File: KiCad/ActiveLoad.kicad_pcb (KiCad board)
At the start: 2 copper layers, 80 x 70 mm, 59 parts, among them J1 AuxPower, J2 TWI, J3 PDI, J4 TC74X-3.3, J5 PowerInput, J6 FAN, Q1 BC807, Q2 BC817, Q4 BD136, U1 LM78L33, U2 L78M12, U3 ATXMEGA32E5-AU, U4 LM358, U5 TL081

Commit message: PCB
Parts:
- removed C1: 47u, Capacitors_SMD:CP_Elec_6.3x5.8
- removed Q1: BC807, TO_SOT_Packages_SMD:SOT-23
- removed R3: 13, Resistors_SMD:R_0805
- added D1: 1N4148, Diodes_SMD:D_1206, B.Cu at (94.6, 87.6)
- added Q3: BD911, TO_SOT_Packages_THT:TO-220-3_Vertical, B.Cu at (81.9, 59.1)
- added ROT1: ROTARY-ENCODER, sparkfun:SF-ROTARY-ENCODER, F.Cu at (104.8, 79.4)
- added SW1: SW_SPDT, JPConnectors:SlideSwitch3Poles, F.Cu at (62.9, 48.9)
- added SW2: SW_SPDT, JPConnectors:SlideSwitch3Poles, F.Cu at (52.7, 74.3)
- C10, C11, C12, C13, C14, C15, C16, C17, C18, C2, C3, C4, C5, C6, C7, C8, C9, J6, L1, Q2, Q4, R1, R10, R11, R12, R13, R14, R15, R16, R17, R18, R19, R2, R20, R21, R22, R23, R26, R4, R5, R6, R7, R8, R9, U2, U3, U4, U5: moved to B.Cu
- J3: footprint Pin_Headers:Pin_Header_Straight_2x03_Pitch2.54mm -> Pin_Headers:Pin_Header_Angled_2x03_Pitch2.54mm; moved to B.Cu
- U1: value LM78L33 -> UA78M33; footprint TO_SOT_Packages_SMD:SOT-89-3 -> TO_SOT_Packages_SMD:TO-252-2; moved to B.Cu
- moved C2 160.5 mm to (54.0, 92.7), turned to 90 degrees
- moved C10 147.5 mm to (76.8, 95.9), turned to 90 degrees
- moved R14 146.7 mm to (75.6, 78.7), turned to 270 degrees
- moved R1 146.3 mm to (75.6, 69.8), turned to 180 degrees
- moved C9 141.9 mm to (65.4, 83.8), turned to 270 degrees
- moved R24 130.5 mm to (76.8, 31.8)
- moved C8 128.2 mm to (57.8, 78.1), turned to 270 degrees
- moved R26 127.4 mm to (85.7, 62.9), turned to 270 degrees
- moved C4 126.2 mm to (46.4, 84.5), turned to 180 degrees
- moved C16 124.9 mm to (92.1, 61.0), turned to 180 degrees
- moved U5 124.7 mm to (90.8, 64.8), turned to 180 degrees
- moved C5 123.1 mm to (89.5, 105.4), turned to 90 degrees
- moved C15 122.8 mm to (82.5, 83.8)
- moved R15 120.3 mm to (96.5, 62.9), turned to 90 degrees
- moved R25 120.0 mm to (76.2, 27.9)
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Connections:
- U1 pad 1: +3V3 -> Net-(C4-Pad1)
- U1 pad 3: Net-(C1-Pad1) -> +3V3
- U3 pad 11: Net-(U3-Pad11) -> ENC_A
- U3 pad 12: Net-(U3-Pad12) -> ENC_B
- U3 pad 29: Net-(U3-Pad29) -> CURRENT_LEVEL
- U3 pad 3: FAN_CONTROL -> DRAIN_CONTROL
- U3 pad 30: Net-(U3-Pad30) -> VOLTAGE_LEVEL
- U3 pad 4: DRAIN_CONTROL -> FAN_CONTROL
- U3 pad 9: Net-(U3-Pad9) -> ENC_Switch
- U4 pad 1: Net-(R16-Pad2) -> Net-(R12-Pad1)
- U4 pad 2: Net-(C14-Pad1) -> Net-(R13-Pad2)
- U4 pad 3: Net-(R12-Pad2) -> Net-(R17-Pad2)
- U4 pad 5: Net-(R17-Pad2) -> Net-(R12-Pad2)
- U4 pad 6: Net-(R13-Pad2) -> Net-(C14-Pad1)
- U4 pad 7: Net-(R12-Pad1) -> Net-(R16-Pad2)
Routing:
- net GND: track 0.00 -> 233.9 mm
- net +3V3: track 0.00 -> 142.0 mm, vias 0 -> 2
- net PowerInput: track 0.00 -> 76.6 mm
- net +12V: track 0.00 -> 72.1 mm, vias 0 -> 1
- net SDA: track 0.00 -> 68.0 mm, vias 0 -> 2
- net SCK: track 0.00 -> 66.5 mm, vias 0 -> 3
- net Net-(C4-Pad1): track 0.00 -> 53.5 mm
- net CURRENT_LEVEL: track 0.00 -> 41.7 mm
- net Net-(C18-Pad1): track 0.00 -> 41.5 mm
- net FAN_CONTROL: track 0.00 -> 38.0 mm, vias 0 -> 2
- net ENC_Switch: track 0.00 -> 31.1 mm
- net PDI_DATA: track 0.00 -> 26.2 mm, vias 0 -> 1
- net ENC_B: track 0.00 -> 24.7 mm
- net PDI_CLK: track 0.00 -> 21.9 mm, vias 0 -> 1
- net ENC_A: track 0.00 -> 20.6 mm
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- added copper zone on B.Cu, net GND
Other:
- net class Default: trace_width 0.25 -> 0.5; via_dia 0.6 -> 1.4; via_drill 0.4 -> 0.6
- net class HighCurrent added: clearance 0.3, trace_width 2, via_dia 2.4, via_drill 1
- net class Power added: clearance 0.2, trace_width 1, via_dia 1.6, via_drill 0.8

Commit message: Finishing touches
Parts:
- added REF**: MountingHole_3.5mm, Mounting_Holes:MountingHole_3.5mm, F.Cu at (48.5, 105.4)
- added REF**: MountingHole_3.5mm, Mounting_Holes:MountingHole_3.5mm, F.Cu at (109.0, 44.0)
- added REF**: MountingHole_3.5mm, Mounting_Holes:MountingHole_3.5mm, F.Cu at (48.5, 44.0)
- added REF**: MountingHole_3.5mm, Mounting_Holes:MountingHole_3.5mm, F.Cu at (109.0, 105.4)
- R20: footprint Resistors_THT:R_Axial_Power_L48.0mm_W12.5mm_P55.88mm -> JPResistors:R_Axial_Power_L48.0mm_W12.5mm_P50.8mm
- R24, R25: moved to B.Cu
- U1, U2: footprint TO_SOT_Packages_SMD:TO-252-2 -> TO_SOT_Packages_SMD:TO-252-2_Rectifier
- moved R25 74.9 mm to (74.9, 102.9), turned to 90 degrees
- moved R24 68.6 mm to (74.3, 100.3), turned to 180 degrees
- moved C9 3.81 mm to (65.4, 80.0)
- moved SW1 2.54 mm to (65.4, 48.9)
- moved R20 2.01 mm to (53.3, 49.5)
- moved C4 1.91 mm to (48.3, 84.5)
- moved J3 1.91 mm to (106.7, 99.1)
- moved C2 0.63 mm to (54.6, 92.7)
- moved J1 0.63 mm to (43.2, 63.5)
- moved J5 0.63 mm to (116.8, 63.5)
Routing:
- net GND: track 233.9 -> 386.3 mm, vias 0 -> 3
- net CURRENT_LEVEL: track 41.7 -> 111.2 mm, vias 0 -> 1
- net PowerInput: track 76.6 -> 130.9 mm, vias 0 -> 1
- net +3V3: track 142.0 -> 171.4 mm, vias 2 -> 5
- net Net-(J1-Pad2): track 19.9 -> 32.7 mm
- net VOLTAGE_LEVEL: track 0.00 -> 6.09 mm
- net Net-(C16-Pad1): track 5.98 -> 7.62 mm
- net +12V: track 72.1 -> 71.4 mm, vias 1 -> 2
- net Net-(C4-Pad1): track 53.5 -> 52.9 mm
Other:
- board text added: "0R1 15W"
- board text added: "ActiveLoad v1 2018.03.18, JP"
- board text added: "Aux Power"
- board text added: "Gnd"
- board text added: "Input Power"
- board text added: "bypass"

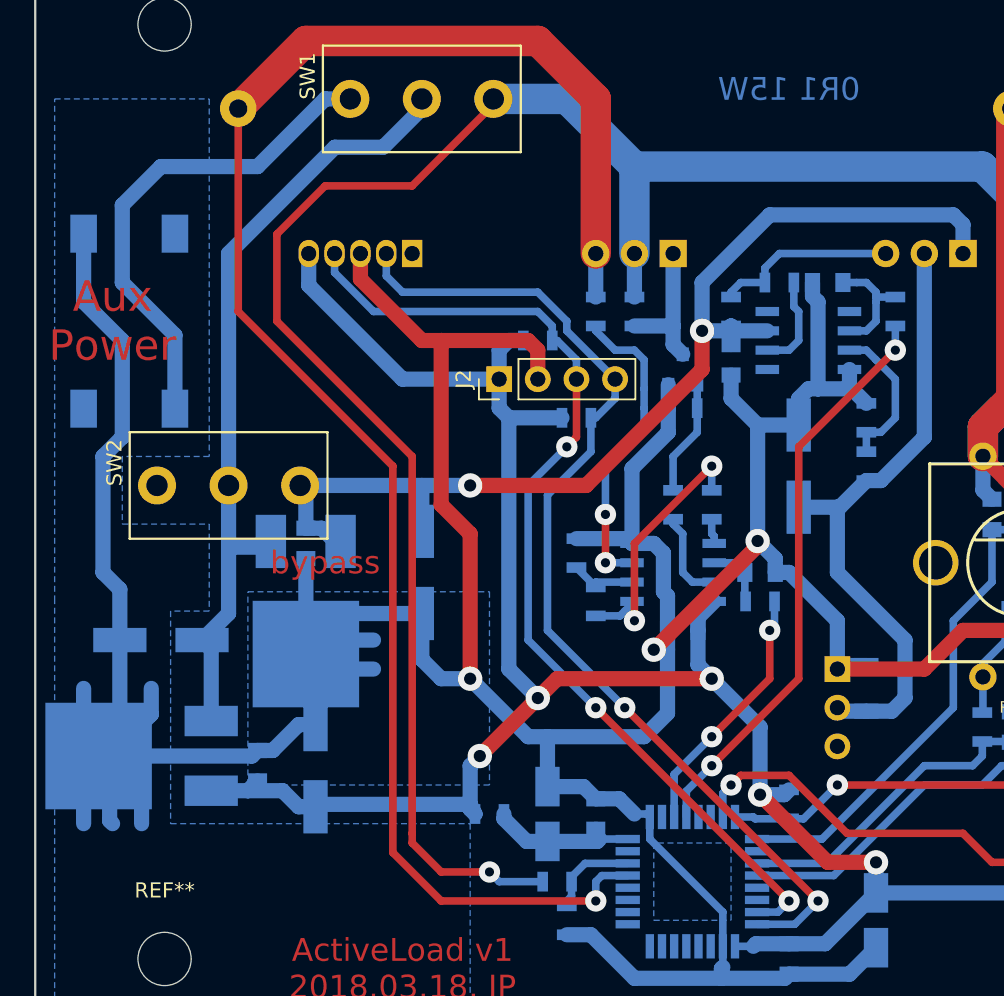
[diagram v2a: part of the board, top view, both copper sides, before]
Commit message: Diodes around 7812 added
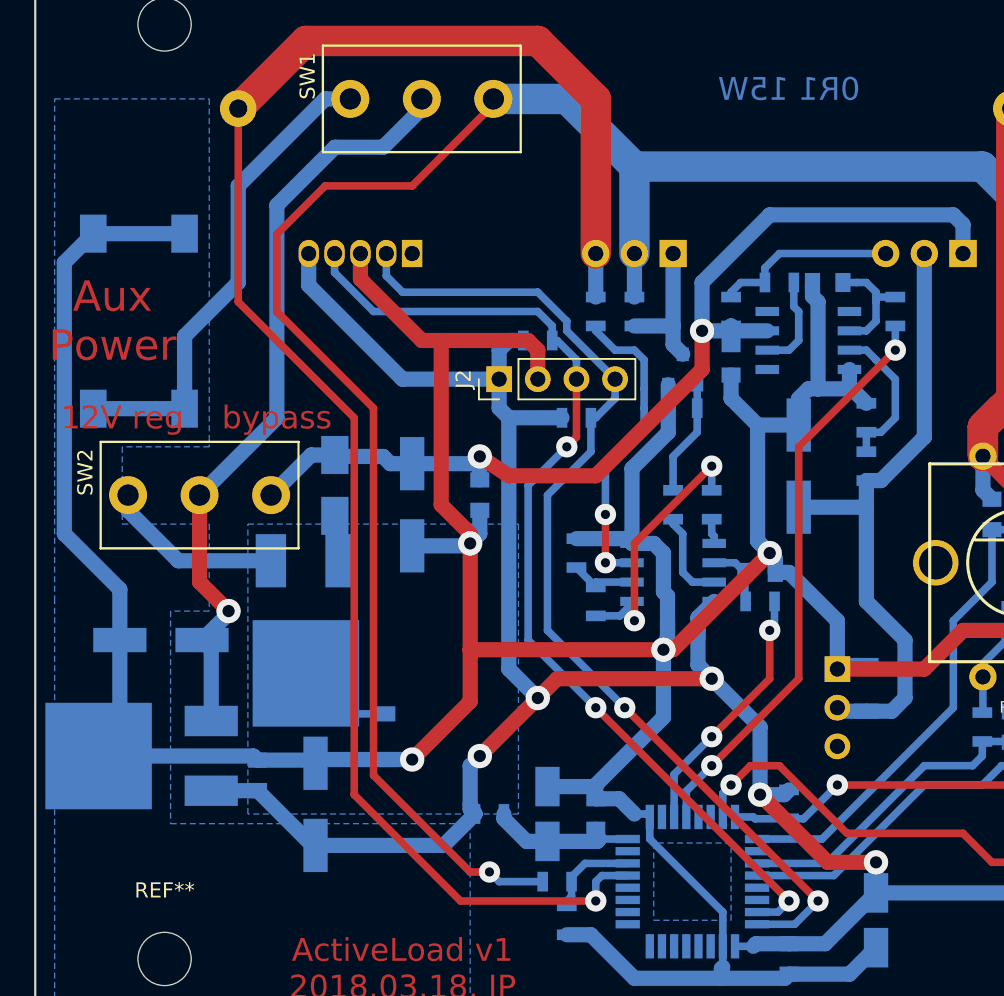
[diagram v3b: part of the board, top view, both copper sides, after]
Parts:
- added D2: 1N4148, Diodes_SMD:D_1206, B.Cu at (62.9, 90.8)
- added D3: BYS10-45, Diodes_SMD:D_SMA, B.Cu at (59.7, 74.3)
- moved C8 11.9 mm to (69.2, 74.9)
- moved C9 4.49 mm to (64.8, 75.6)
- moved C3 2.54 mm to (58.4, 95.2)
- moved SW2 2.01 mm to (50.8, 74.9)
- moved U2 1.27 mm to (57.8, 83.8)
- moved C2 0.64 mm to (54.6, 93.3)
- moved J1 0.63 mm to (43.8, 63.5)
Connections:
- U2 pad 1: Net-(C4-Pad1) -> Net-(SW2-Pad3)
- U2 pad 2: GND -> Net-(D2-Pad2)
- U2 pad 3: +12V -> Net-(D3-Pad2)
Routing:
- net GND: track 386.3 -> 355.7 mm, vias 3 -> 4
- net Net-(SW2-Pad3): track 0.00 -> 11.8 mm
- net Net-(D2-Pad2): track 0.00 -> 10.0 mm
- net +12V: track 71.4 -> 67.7 mm
- net Net-(D3-Pad2): track 0.00 -> 3.50 mm
- net Net-(C4-Pad1): track 52.9 -> 50.8 mm, vias 0 -> 1
- net PowerInput: track 130.9 -> 129.8 mm
- net +3V3: track 171.4 -> 172.5 mm
- net Net-(J1-Pad2): track 32.7 -> 31.8 mm
- net CURRENT_LEVEL: track 111.2 -> 110.5 mm
- net PDI_DATA: track 25.9 -> 26.4 mm
- added copper zone on B.Cu, net Net-(D2-Pad2)
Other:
- board text added: "12V reg"

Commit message: Finishing touches
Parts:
- added REF**: MountingHole_4mm, Mounting_Holes:MountingHole_4mm, F.Cu at (119.4, 52.7)
- added REF**: MountingHole_4mm, Mounting_Holes:MountingHole_4mm, F.Cu at (119.4, 82.5)
- J2: footprint Pin_Headers:Pin_Header_Straight_1x04_Pitch2.54mm -> JPDisplays:OLED_0.96inch_128x64_I2C
- moved R25 47.1 mm to (57.8, 59.1), turned to 270 degrees
- moved R24 45.2 mm to (55.9, 59.1), turned to 90 degrees
- moved J5 7.41 mm to (123.2, 67.3)
- moved J3 5.71 mm to (112.4, 99.1)
- moved J4 2.54 mm to (67.3, 59.1)
- moved C12 1.91 mm to (102.2, 90.2)
- moved C13 1.91 mm to (104.1, 90.2)
- moved C7 1.91 mm to (101.0, 76.2)
- moved R10 1.91 mm to (106.0, 90.2)
- moved R5 1.91 mm to (102.9, 76.2)
- moved R6 1.91 mm to (104.8, 76.2)
- moved R7 1.91 mm to (102.2, 83.2)
- moved R8 1.91 mm to (104.8, 83.2)
- moved R9 1.91 mm to (100.3, 90.2)
- moved ROT1 1.91 mm to (102.9, 79.4)
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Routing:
- net VOLTAGE_LEVEL: track 6.09 -> 58.3 mm, vias 0 -> 2
- net PowerInput: track 129.8 -> 94.9 mm, vias 1 -> 0
- net GND: track 355.7 -> 377.3 mm
- net PDI_DATA: track 26.4 -> 32.1 mm
- net PDI_CLK: track 21.7 -> 27.4 mm
- net SCK: track 66.5 -> 63.9 mm
- net SDA: track 68.0 -> 65.5 mm
- net +3V3: track 172.5 -> 174.6 mm
- net ENC_Switch: track 31.1 -> 30.4 mm
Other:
- board size 80 x 70 mm -> 85.7 x 70 mm
- board text added: "ActiveLoad v1 2018.04.05, JP"
- board text added: "Vdd"
- board text removed: "ActiveLoad v1 2018.03.18, JP"

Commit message: Finishing touches
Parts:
- C11, C6: footprint Capacitors_SMD:CP_Elec_4x5.8 -> Capacitors_SMD:CP_Elec_3x5.3
- D1, D2: footprint Diodes_SMD:D_1206 -> SMD_Packages:SMD-1206_Pol
- J2: value TWI -> OLED I2C
- moved D1 5.43 mm to (92.7, 82.5), turned to 180 degrees
- moved R2 4.62 mm to (68.6, 66.0), turned to 270 degrees
- moved C6 1.80 mm to (94.0, 104.1)
- moved J6 1.27 mm to (94.0, 86.4)
- moved C11 0.64 mm to (74.3, 95.9)
- moved D2 0.64 mm to (62.9, 90.2)
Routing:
- net CURRENT_LEVEL: track 110.1 -> 100.5 mm
- net GND: track 377.3 -> 373.4 mm
- net +3V3: track 174.6 -> 171.3 mm
- net Net-(D2-Pad2): track 10.0 -> 7.03 mm
- net Net-(C18-Pad1): track 41.7 -> 39.7 mm
- net VOLTAGE_LEVEL: track 58.3 -> 57.5 mm
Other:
- board text added: "12V reg / bypass"
- board text added: "Aux / Off / Input"
- board text removed: "12V reg"
- board text removed: "bypass"
